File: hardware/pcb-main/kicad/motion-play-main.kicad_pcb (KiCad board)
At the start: 4 copper layers, 88 x 40 mm, 90 parts, among them IC1 SN74AHCT125PWR, J3 LED_Strip, J4 Conn_01x05, J5 Conn_01x05, J6 Conn_01x05, J7 TYPE-C-31-M-12, J8 JST_PH_2pin, Q2 PMOS, SW1 SS-12D10L5, SW2 RESET, SW3 BOOT, U3 ESP32-S3-WROOM-1-N16R8, U4 TCA9548APWR, U5 BQ24195RGER, U6 TPS61088RHLR, U7 INA219AIDCNR, U8 AMS1117-3.3, U9 USBLC6-2SC6

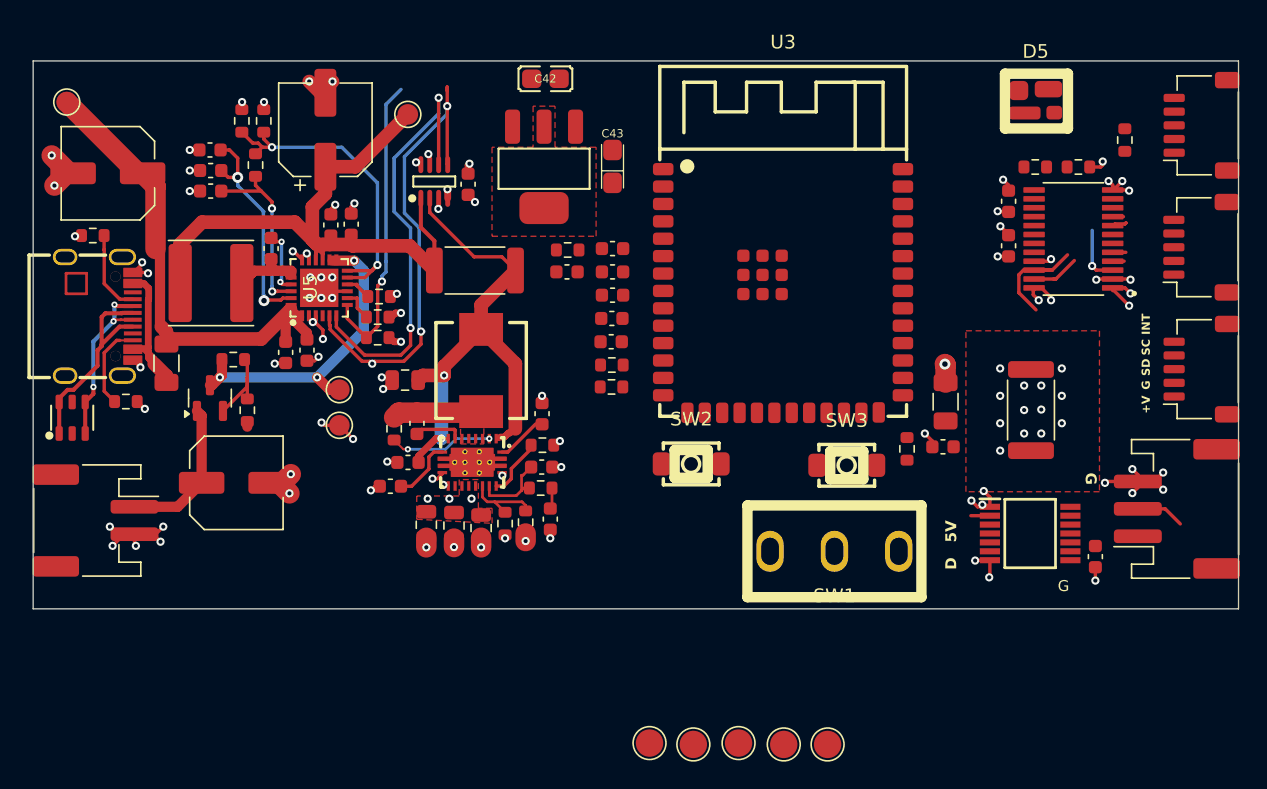
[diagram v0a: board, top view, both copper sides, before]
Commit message: Hardware revision: remove interrupts, update connectors, add DIP switch
Remove INT lines from all three PCBs (main, rigid, flex). Replace 5-pin
JST-SH connectors with 4-pin SM04B-SRSS-TB on main and rigid boards.
Replace solder jumpers with EP-02KS DIP switch for I2C address config
on rigid board. Update FPC connector pinout to remove INT signals and
add GND fills. Update stiffener specs (PI 0.25mm tail, SS 0.2mm IC
areas). Regenerate production files (BOM, CPL) for both sensor boards.
Update hardware CONTEXT.md with corrected addresses (0x74-0x76),
component tables, and pinouts.

Made-with: Cursor
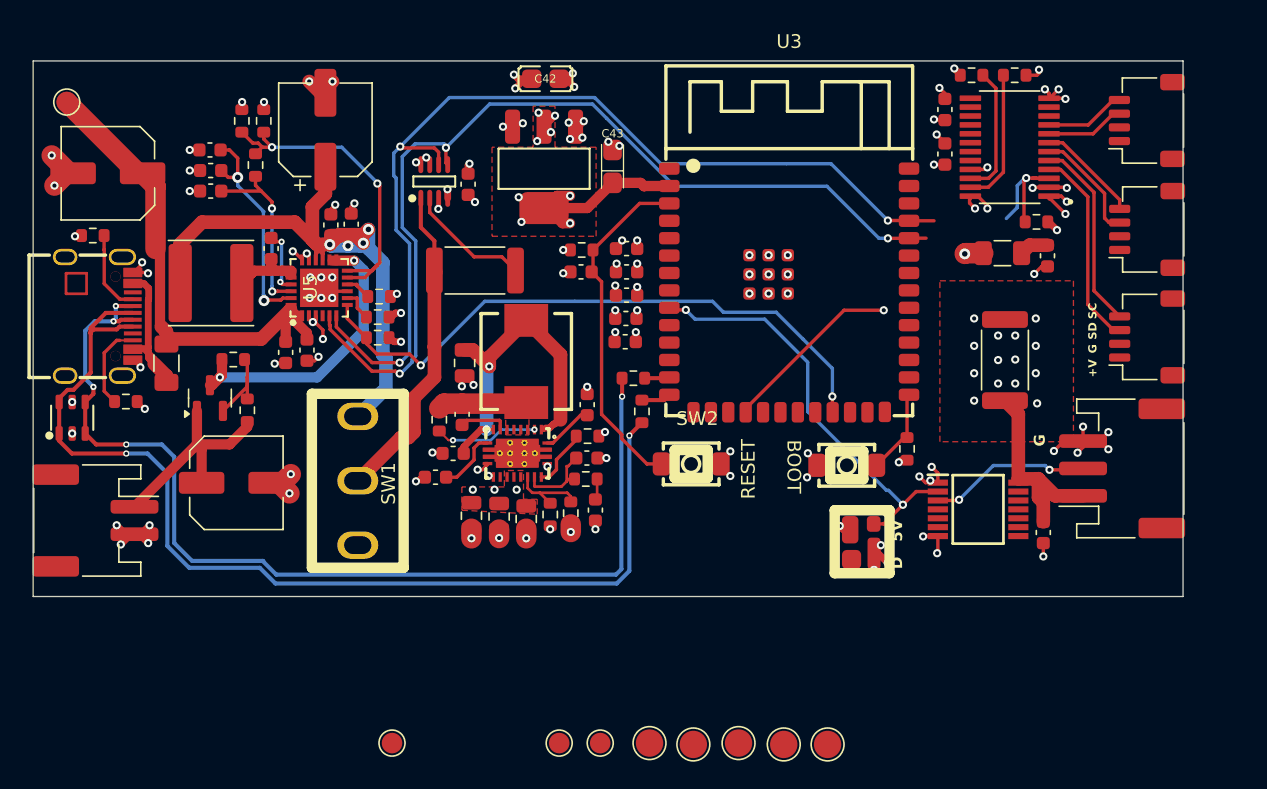
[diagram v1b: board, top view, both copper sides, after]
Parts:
- J4, J5, J6: value Conn_01x05 -> Conn_01x04; footprint Connector_JST:JST_SH_SM05B-SRSS-TB_1x05-1MP_P1.00mm_Horizontal -> Connector_JST:JST_SH_SM04B-SRSS-TB_1x04-1MP_P1.00mm_Horizontal
- moved TP1 45.9 mm to (102.2, 150.8)
- moved SW1 35.2 mm to (99.7, 131.7), turned to -90 degrees
- moved D5 34.7 mm to (136.5, 136.2), turned to 90 degrees
- moved TP2 30.4 mm to (114.4, 150.8)
- moved TP4 30.0 mm to (117.4, 150.8)
- moved C7 15.9 mm to (150.1, 115.2), turned to 90 degrees
- moved F1 11.6 mm to (146.8, 115.0), turned to 0 degrees
- moved R6 8.79 mm to (149.2, 112.8), turned to 0 degrees
- moved C10 8.16 mm to (142.6, 104.5)
- moved C9 8.16 mm to (142.6, 107.8)
- moved R28 8.16 mm to (147.7, 102.0)
- moved R29 8.16 mm to (144.5, 102.0)
- moved U4 8.16 mm to (147.3, 107.3)
- moved J3 4.97 mm to (155.5, 130.8)
- moved J4 4.62 mm to (157.3, 121.2)
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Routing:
- net /USB_DN: track 13.2 -> 75.7 mm, vias 3 -> 5
- net /USB_DP: track 15.4 -> 77.1 mm, vias 0 -> 2
- net /I2C_SDA: track 35.7 -> 81.8 mm, vias 2 -> 3
- net /I2C_SCL: track 43.6 -> 79.2 mm
- net /LED_DATA: track 1.39 -> 31.2 mm, vias 0 -> 2
- net /ESP32_S3/EN: track 0.00 -> 25.4 mm
- net +3.3V: track 9.14 -> 33.9 mm, vias 9 -> 26
- net /Power Management/VSYS_SW: track 0.00 -> 23.8 mm
- net /CHRG_INT: track 22.1 -> 45.2 mm, vias 1 -> 2
- net /TCA_RESET: track 4.22 -> 22.2 mm, vias 1 -> 2
- net /LED Controller/+5V_TO_LEDS: track 0.00 -> 14.7 mm
- net /TCA9548A_Subsystem/CH0_SCL: track 0.96 -> 14.9 mm
- net /TCA9548A_Subsystem/CH0_SDA: track 0.84 -> 14.6 mm
- net GND: track 80.6 -> 93.1 mm, vias 92 -> 122
- net /TCA9548A_Subsystem/CH1_SDA: track 0.00 -> 8.36 mm
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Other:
- board size 88 x 40 mm -> 83.9 x 39.1 mm
- board text added: "BOOT"
- board text added: "RESET"
- board text removed: "INT"

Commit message: Fixed polarity protection on the power circuit
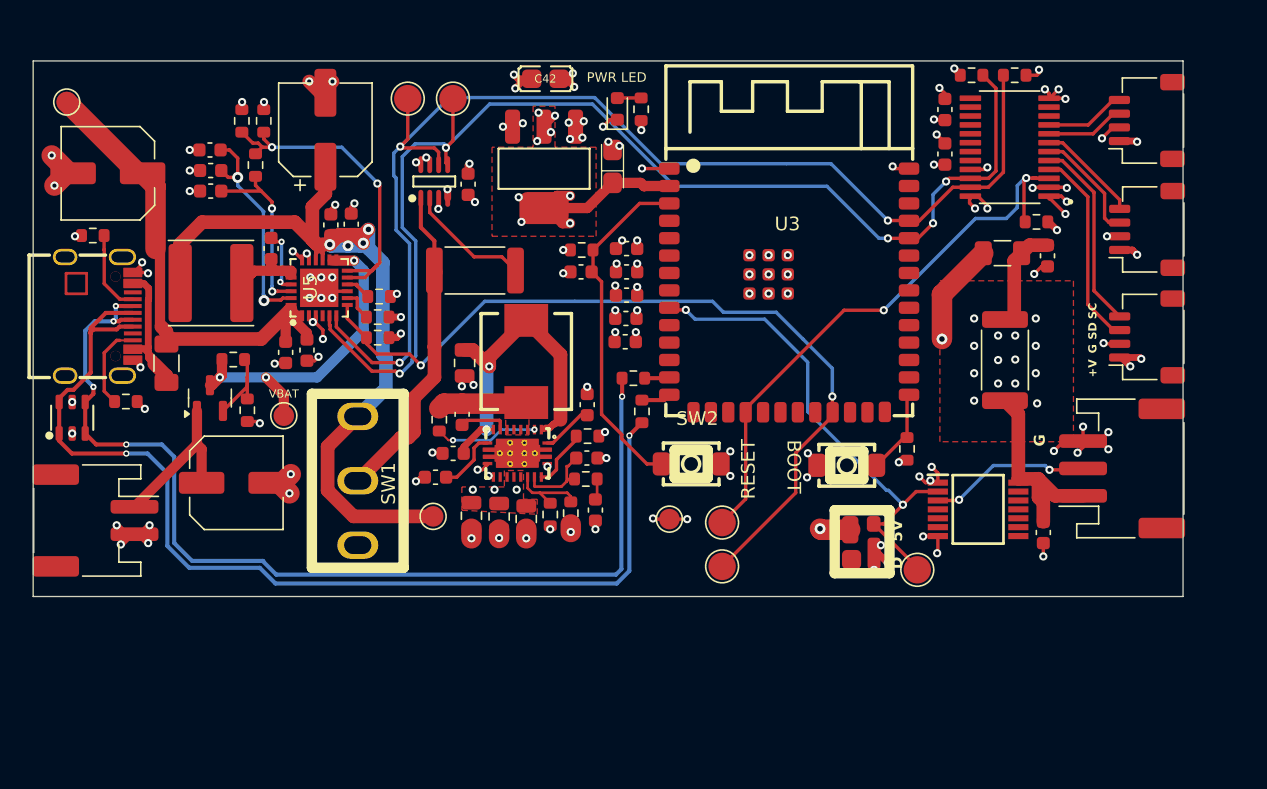
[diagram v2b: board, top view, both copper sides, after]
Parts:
- added D1: LED, LED_SMD:LED_0603_1608Metric, F.Cu at (118.7, 104.5)
- added R1: 1kΩ, Resistor_SMD:R_0603_1608Metric, F.Cu at (120.4, 104.5)
- moved TPIO43 54.6 mm to (103.3, 103.8), turned to 90 degrees
- moved TPIO44 51.5 mm to (106.7, 103.8), turned to 90 degrees
- moved TP2 31.2 mm to (94.3, 126.9)
- moved TP4 17.1 mm to (122.5, 134.4)
- moved TP1 16.8 mm to (105.2, 134.2)
- moved TPIO10 16.3 mm to (126.3, 134.7)
- moved TPIO16 14.3 mm to (140.6, 138.2)
- moved TPIO21 13.9 mm to (126.3, 137.9)
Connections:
- R34 pad 2: /Power Management/BAT_RAW -> GND
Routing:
- net /TCA_RESET: track 22.2 -> 42.7 mm
- net /Power Management/VSYS: track 52.2 -> 67.0 mm
- net /CHRG_INT: track 45.2 -> 59.8 mm
- net GND: track 93.1 -> 104.9 mm, vias 122 -> 131
- net /I2C_SCL: track 79.2 -> 89.3 mm, vias 3 -> 5
- net +5V: track 7.26 -> 14.8 mm
- net /I2C_SDA: track 81.8 -> 89.2 mm
- net +3.3V: track 33.9 -> 40.0 mm, vias 26 -> 31
- net Net-(C7-Pad2): track 2.81 -> 7.87 mm
- net /LED_DATA: track 31.2 -> 35.8 mm
- net /Power Management/BAT_RAW: track 16.4 -> 11.8 mm
- net /Power Management/VBAT: track 21.2 -> 24.6 mm, vias 2 -> 3
- net Net-(D1-A): track 0.00 -> 1.74 mm
